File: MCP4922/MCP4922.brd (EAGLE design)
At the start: 33.5 x 31 mm, 27 parts, among them U1 MCP4922, U2 MCP4922, U3 LM4040D50IDBZR

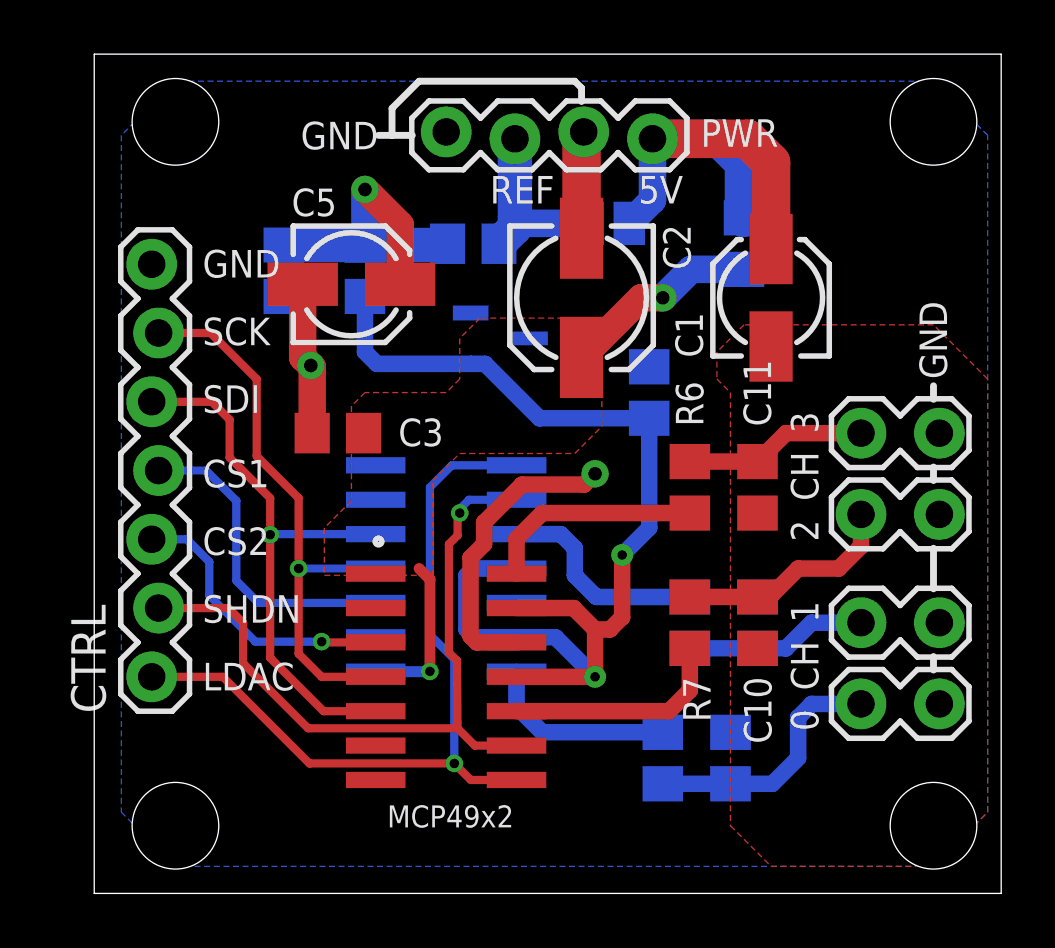
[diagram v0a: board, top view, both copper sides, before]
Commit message: Added jumper for voltage reference; readme
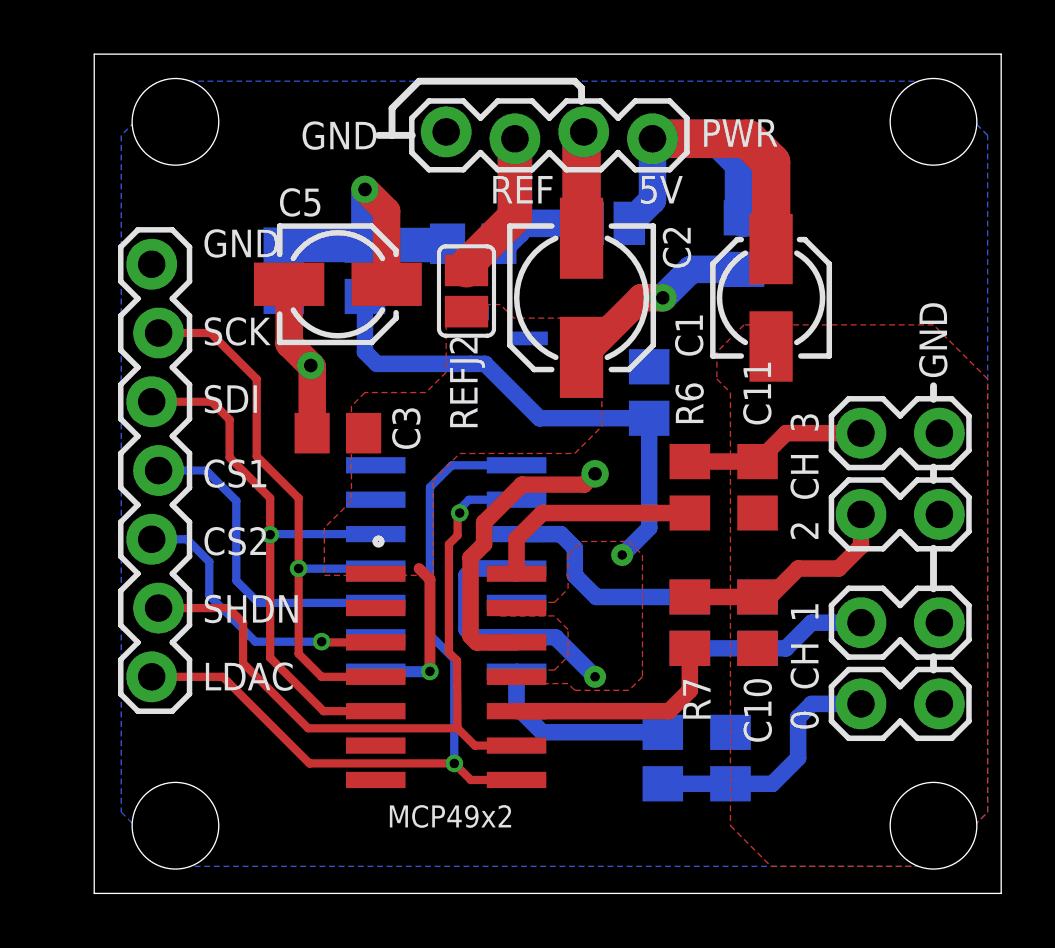
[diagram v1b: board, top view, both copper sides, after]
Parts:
- added REFJ2: (no value), jumper:SJ
- moved C5 0.50 mm to (9.00, 22.5)
- renumbered REFJ to REFJ1
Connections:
- net +5V: now also REFJ2.2
- net N$10: now also REFJ2.1
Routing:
- net VREF: track 39.8 -> 28.5 mm
- net N$10: track 6.92 -> 12.5 mm
- added copper zone on layer 1, net VREF
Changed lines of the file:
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@@
 <text x="4" y="10" size="1.016" layer="21" ratio="10">SHDN</text>
 <text x="4" y="7.5" size="1.016" layer="21" ratio="10">LDAC</text>
-<text x="4" y="22.75" size="1.016" layer="21" ratio="10">GND</text>
+<text x="4" y="23.5" size="1.016" layer="21" ratio="10">GND</text>
 <text x="10.5" y="28.5" size="1.016" layer="21" ratio="10" rot="R180">GND</text>
 <text x="17" y="26.5" size="1.016" layer="21" ratio="10" rot="R180">REF</text>
@@
 </element>
 <element name="C3" library="rcl" package="C0805" value="" x="9" y="17" smashed="yes" rot="R180">
-<attribute name="NAME" x="11.23" y="16.52" size="1.016" layer="25"/>
+<attribute name="NAME" x="11.02" y="18.02" size="1.016" layer="25" rot="R270"/>
 <attribute name="VALUE" x="10.27" y="19.54" size="1.27" layer="27" rot="R180"/>
 </element>
@@
 <attribute name="VALUE" x="9.54" y="24.27" size="1.27" layer="28" rot="MR270"/>
 </element>
-<element name="C5" library="rcl" package="153CLV-0405" value="" x="9.5" y="22.5" smashed="yes">
-<attribute name="NAME" x="7.29" y="25.016" size="1.016" layer="25" ratio="10"/>
-<attribute name="VALUE" x="12.04" y="20.341" size="1.27" layer="27" ratio="10"/>
+<element name="C5" library="rcl" package="153CLV-0405" value="" x="9" y="22.5" smashed="yes">
+<attribute name="NAME" x="6.79" y="25.016" size="1.016" layer="25" ratio="10"/>
+<attribute name="VALUE" x="11.54" y="20.341" size="1.27" layer="27" ratio="10"/>
 </element>
 <element name="U3" library="LM4040-5.0_SOIC" package="SOT95P237X112-3N" value="LM4040D50IDBZR" x="15" y="20.5" smashed="yes" rot="MR180">
@@
 <element name="JP3" library="SparkFun-Connectors" package="1X02_LOCK" value="M02LOCK" x="28.5" y="17" smashed="yes"/>
 <element name="JP4" library="SparkFun-Connectors" package="1X02_LOCK" value="M02LOCK" x="28.5" y="14" smashed="yes"/>
-<element name="REFJ" library="jumper" package="SJ" value="" x="19" y="24.75" smashed="yes" rot="MR180">
-<attribute name="NAME" x="16.849" y="23.607" size="1.016" layer="26" ratio="10" rot="MR180"/>
+<element name="REFJ1" library="jumper" package="SJ" value="" x="19" y="24.75" smashed="yes" rot="MR180">
+<attribute name="NAME" x="16.349" y="23.607" size="1.016" layer="26" ratio="10" rot="MR180"/>
 <attribute name="VALUE" x="19.4001" y="24.75" size="0.02" layer="28" rot="MR180"/>
 </element>
-<element name="CTRL" library="SparkFun-Connectors" package="1X07_LOCK" value="" x="2.25" y="8" rot="R90"/>
+<element name="CTRL" library="SparkFun-Connectors" package="1X07_LOCK" value="" x="2.25" y="8" smashed="yes" rot="R90">
+<attribute name="VALUE" x="5.425" y="6.73" size="1.27" layer="27" rot="R90"/>
+</element>
+<element name="REFJ2" library="jumper" package="SJ" value="" x="13.75" y="22.25" smashed="yes" rot="R270">
+<attribute name="NAME" x="13.143" y="20.651" size="1.016" layer="25" ratio="10" rot="R270"/>
+<attribute name="VALUE" x="13.75" y="21.8499" size="0.02" layer="27" rot="R270"/>
+</element>
 </elements>
 <signals>
@@
 <via x="18.5" y="15.5" extent="1-16" drill="0.5" diameter="1.016"/>
 <wire x1="18.1" y1="15.1" x2="18.5" y2="15.5" width="0.6096" layer="1"/>
-<wire x1="7.7" y1="22.5" x2="7.7" y2="19.8" width="1.016" layer="1"/>
-<wire x1="7.7" y1="19.8" x2="8" y2="19.5" width="1.016" layer="1"/>
+<wire x1="7.2" y1="22.5" x2="7.2" y2="20.3" width="1.016" layer="1"/>
+<wire x1="7.2" y1="20.3" x2="8" y2="19.5" width="1.016" layer="1"/>
 <contactref element="CTRL" pad="7"/>
 </signal>
@@
 <wire x1="14.4398" y1="19.5602" x2="16.45" y2="17.55" width="0.6096" layer="16"/>
 <wire x1="20.5" y1="17.55" x2="16.45" y2="17.55" width="0.6096" layer="16"/>
-<wire x1="15.6" y1="8" x2="18.5" y2="8" width="0.6096" layer="1"/>
 <via x="18.5" y="8" extent="1-16" drill="0.35" diameter="0.8128"/>
 <wire x1="15.6" y1="9.46" x2="17.04" y2="9.46" width="0.6096" layer="16"/>
 <wire x1="17.04" y1="9.46" x2="18.5" y2="8" width="0.6096" layer="16"/>
-<wire x1="15.6" y1="10.54" x2="17.71" y2="10.54" width="0.6096" layer="1"/>
-<wire x1="17.71" y1="10.54" x2="18.5" y2="9.75" width="0.6096" layer="1"/>
-<wire x1="18.5" y1="9.75" x2="18.5" y2="8" width="0.6096" layer="1"/>
 <wire x1="15.6" y1="12" x2="14" y2="12" width="0.6096" layer="16"/>
 <wire x1="14" y1="12" x2="13.75" y2="11.75" width="0.6096" layer="16"/>
@@
 <wire x1="15.6" y1="9.46" x2="14.04" y2="9.46" width="0.6096" layer="16"/>
 <via x="19.5" y="12.5" extent="1-16" drill="0.35" diameter="0.8128"/>
-<wire x1="19.5" y1="12.5" x2="19.5" y2="10.2" width="0.6096" layer="1"/>
-<wire x1="19.5" y1="10.2" x2="19.05" y2="9.75" width="0.6096" layer="1"/>
-<wire x1="18.5" y1="9.75" x2="19.05" y2="9.75" width="0.6096" layer="1"/>
 <wire x1="20.5" y1="17.55" x2="20.5" y2="13.5" width="0.6096" layer="16"/>
 <wire x1="20.5" y1="13.5" x2="19.5" y2="12.5" width="0.6096" layer="16"/>
+<polygon width="0.254" layer="1" isolate="0.3048" thermals="no">
+<vertex x="19.75" y="13"/>
+<vertex x="20.25" y="12.5"/>
+<vertex x="20.25" y="8"/>
+<vertex x="19.75" y="7.5"/>
+<vertex x="17.75" y="7.5"/>
+<vertex x="17.5" y="7.75"/>
+<vertex x="15" y="7.75"/>
+<vertex x="15" y="8.25"/>
+<vertex x="17" y="8.25"/>
+<vertex x="17.5" y="8.75"/>
+<vertex x="17.5" y="9.75"/>
+<vertex x="17" y="10.25"/>
+<vertex x="15" y="10.25"/>
+<vertex x="15" y="10.75"/>
+<vertex x="17" y="10.75"/>
+<vertex x="17.5" y="11.25"/>
+<vertex x="17.5" y="12.5"/>
+<vertex x="18" y="13"/>
+</polygon>
 </signal>
 <signal name="N$1">
@@
 <vertex x="18.75" y="17.25"/>
 <vertex x="18.75" y="21.25"/>
-<vertex x="14.25" y="21.25"/>
-<vertex x="13.5" y="20.5"/>
-<vertex x="13.5" y="19"/>
-<vertex x="13" y="18.5"/>
+<vertex x="15.5" y="21.25"/>
+<vertex x="15" y="21.75"/>
+<vertex x="13" y="21.75"/>
+<vertex x="13" y="19.25"/>
+<vertex x="12.25" y="18.5"/>
 <vertex x="10" y="18.5"/>
 <vertex x="9.5" y="18"/>
@@
 </polygon>
 <wire x1="12.4" y1="11.6" x2="12" y2="12" width="0.4064" layer="1"/>
+<contactref element="REFJ2" pad="2"/>
 </signal>
 <signal name="N$9">
@@
 <wire x1="25" y1="27" x2="24.127" y2="27.873" width="1.4224" layer="1"/>
 <wire x1="24.127" y1="27.873" x2="20.62" y2="27.873" width="1.4224" layer="1"/>
-<contactref element="REFJ" pad="2"/>
+<contactref element="REFJ1" pad="2"/>
 <wire x1="20.62" y1="27.873" x2="20.62" y2="25.608" width="1.016" layer="16"/>
 <wire x1="20.62" y1="25.608" x2="19.762" y2="24.75" width="1.016" layer="16"/>
@@
 <wire x1="15.54" y1="25" x2="15.54" y2="24.59" width="1.27" layer="16"/>
 <wire x1="15.54" y1="24.59" x2="14.95" y2="24" width="1.27" layer="16"/>
-<contactref element="REFJ" pad="1"/>
+<contactref element="REFJ1" pad="1"/>
 <wire x1="18.238" y1="24.75" x2="15.79" y2="24.75" width="1.016" layer="16"/>
 <wire x1="15.79" y1="24.75" x2="15.54" y2="25" width="1.016" layer="16"/>
+<contactref element="REFJ2" pad="1"/>
+<wire x1="13.75" y1="23.012" x2="13.75" y2="23.21" width="1.27" layer="1"/>
+<wire x1="13.75" y1="23.21" x2="15.54" y2="25" width="1.27" layer="1"/>
+<wire x1="15.54" y1="25" x2="15.54" y2="27.873" width="1.27" layer="1"/>
 </signal>
 <signal name="V+">
@@
 <via x="10" y="26" extent="1-16" drill="0.5" diameter="1.016"/>
 <wire x1="10" y1="23.95" x2="10" y2="26" width="1.016" layer="16"/>
-<wire x1="11.3" y1="22.5" x2="11.3" y2="24.7" width="1.016" layer="1"/>
-<wire x1="11.3" y1="24.7" x2="10" y2="26" width="1.016" layer="1"/>
+<wire x1="10.8" y1="22.5" x2="10.8" y2="25.2" width="1.016" layer="1"/>
+<wire x1="10.8" y1="25.2" x2="10" y2="26" width="1.016" layer="1"/>
 </signal>
 <signal name="CS2">
